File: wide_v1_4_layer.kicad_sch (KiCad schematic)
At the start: 10 parts

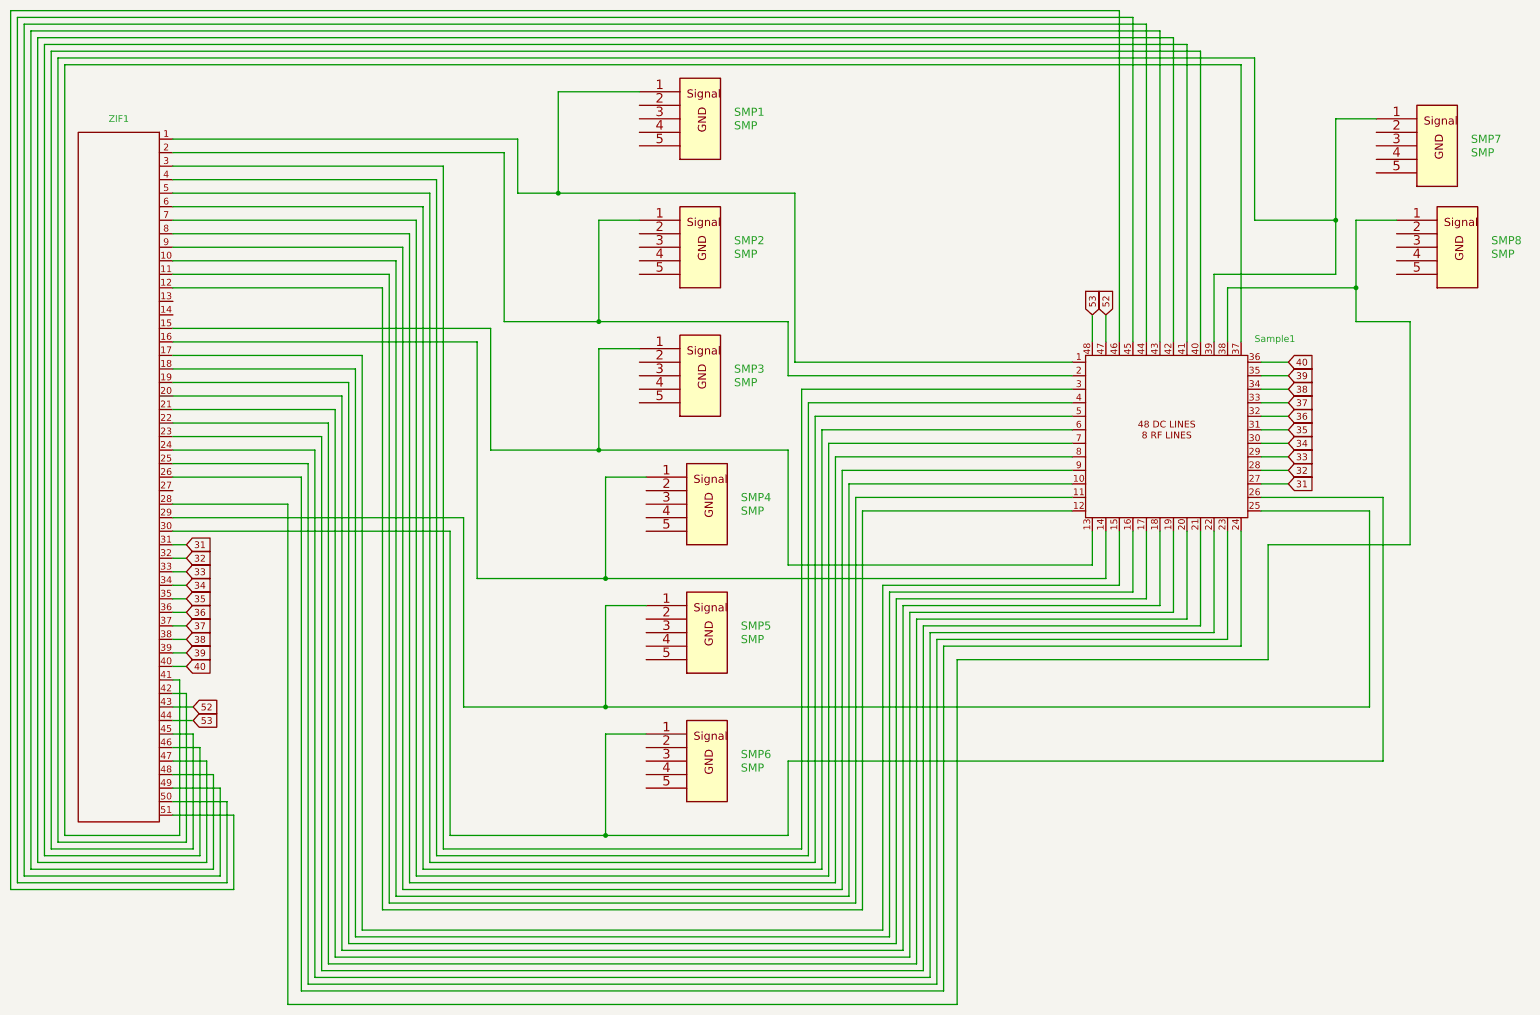
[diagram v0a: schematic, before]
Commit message: removed extra smps, added bias tees
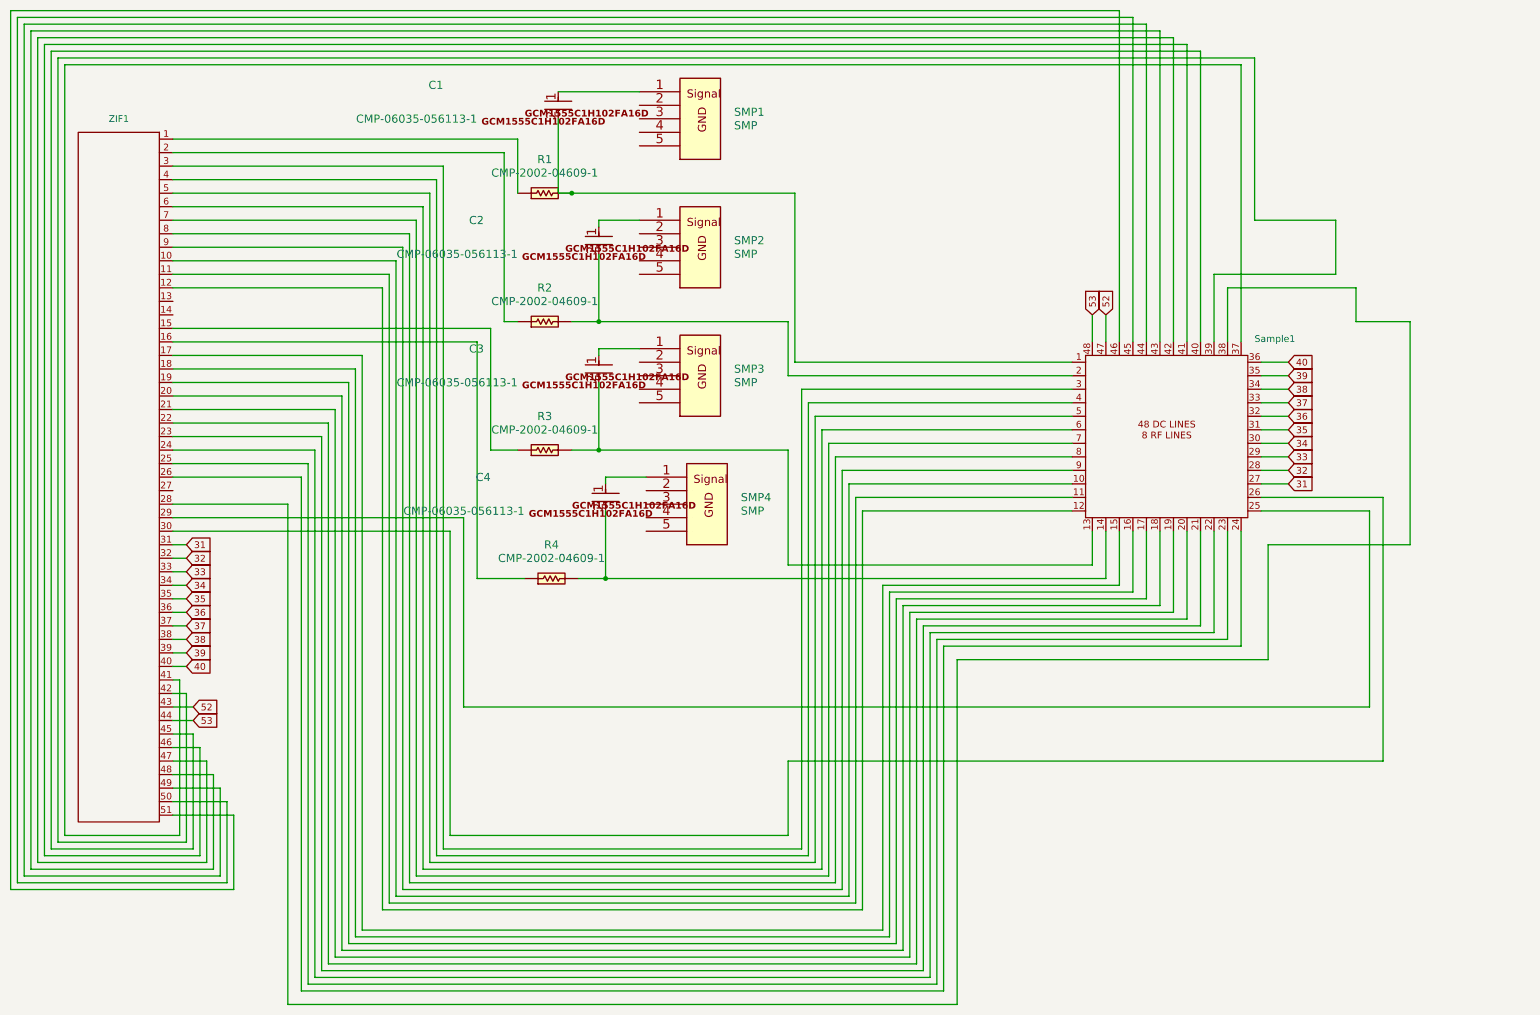
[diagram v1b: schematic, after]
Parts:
- removed SMP5, SMP6, SMP7, SMP8: SMP, PcbLib_narrow_v2:581-M25-113L461, symbol carrier:SMP
- added C1, C2, C3, C4: CMP-06035-056113-1, PcbLib_narrow_v2:CAPC1005X06N, symbol carrier:CMP-06035-056113-1
- added R1, R2, R3, R4: CMP-2002-04609-1, PcbLib_narrow_v2:RESC1005X04N, symbol carrier:CMP-2002-04609-1
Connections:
- new net: C3.1, SMP3.1
- new net: C3.2, R3.2, Sample1.13
- new net: C1.1, SMP1.1
- new net: R2.1, ZIF1.2
- new net: C2.2, R2.2, Sample1.2
- new net: C4.1, SMP4.1
- new net: R3.1, ZIF1.15
- new net: R4.1, ZIF1.16
- new net: C4.2, R4.2, Sample1.14
- new net: R1.1, ZIF1.1
- new net: C1.2, R1.2, Sample1.1
- new net: C2.1, SMP2.1
